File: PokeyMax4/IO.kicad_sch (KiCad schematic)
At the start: 2 parts

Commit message: Update the v4 board
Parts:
- R6: JLCPCB Part # C102771 -> (none); LCSC Part # (none) -> C25860
- R7: JLCPCB Part # C304991 -> (none); LCSC Part # (none) -> C25879
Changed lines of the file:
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@@
+	(wire
+		(pts
+			(xy 144.78 83.82) (xy 144.78 91.44)
+		)
+		(stroke
+			(width 0.1524)
+			(type solid)
+		)
+	)
+	(wire
+		(pts
+			(xy 144.78 119.38) (xy 144.78 121.92)
+		)
+		(stroke
+			(width 0.1524)
+			(type solid)
+		)
+	)
 	(wire
 		(pts
@@
 			(width 0.1524)
 			(type solid)
-		)
-	)
-	(wire
-		(pts
-			(xy 144.78 83.82) (xy 144.78 91.44)
-		)
-		(stroke
-			(width 0.1524)
-			(type solid)
-		)
-	)
-	(wire
-		(pts
-			(xy 144.78 119.38) (xy 144.78 121.92)
-		)
-		(stroke
-			(width 0.1524)
-			(type solid)
-		)
-	)
-	(global_label "3V3"
-		(shape bidirectional)
-		(at 144.78 83.82 0)
-		(fields_autoplaced yes)
-		(effects
-			(font
-				(size 1.2446 1.2446)
-			)
-			(justify left)
-		)
-		(property "Intersheetrefs" "${INTERSHEET_REFS}"
-			(at 152.2316 83.82 0)
-			(effects
-				(font
-					(size 1.27 1.27)
-				)
-				(justify left)
-				(hide yes)
-			)
 		)
 	)
@@
 				(justify left)
 				(hide yes)
+			)
+		)
+	)
+	(global_label "3V3"
+		(shape bidirectional)
+		(at 144.78 87.63 0)
+		(fields_autoplaced yes)
+		(effects
+			(font
+				(size 1.2446 1.2446)
+			)
+			(justify left)
+		)
+		(property "Intersheetrefs" "${INTERSHEET_REFS}"
+			(at 152.2316 87.63 0)
+			(effects
+				(font
+					(size 1.27 1.27)
+				)
+				(justify left)
+				(hide yes)
+			)
+		)
+	)
+	(symbol
+		(lib_id "pokeymax4-eagle-import:R-EU_R0402")
+		(at 144.78 96.52 90)
+		(unit 1)
+		(exclude_from_sim no)
+		(in_bom yes)
+		(on_board yes)
+		(dnp no)
+		(property "Reference" "R6"
+			(at 143.2814 100.33 0)
+			(effects
+				(font
+					(size 1.778 1.5113)
+				)
+				(justify left bottom)
+			)
+		)
+		(property "Value" "1k1"
+			(at 148.082 100.33 0)
+			(effects
+				(font
+					(size 1.778 1.5113)
+				)
+				(justify left bottom)
+			)
+		)
+		(property "Footprint" "pokeymax4:R0402"
+			(at 144.78 96.52 0)
+			(effects
+				(font
+					(size 1.27 1.27)
+				)
+				(hide yes)
+			)
+		)
+		(property "Datasheet" ""
+			(at 144.78 96.52 0)
+			(effects
+				(font
+					(size 1.27 1.27)
+				)
+				(hide yes)
+			)
+		)
+		(property "Description" ""
+			(at 144.78 96.52 0)
+			(effects
+				(font
+					(size 1.27 1.27)
+				)
+				(hide yes)
+			)
+		)
+		(property "LCSC Part #" "C25860"
+			(at 144.78 96.52 0)
+			(effects
+				(font
+					(size 1.27 1.27)
+				)
+				(hide yes)
+			)
+		)
+		(pin "1"
+		)
+		(pin "2"
+		)
+		(instances
+			(project ""
+				(path "/e6275eb3-d183-4a15-8a8c-dffc95cf456c/ffebd24f-75aa-4e21-be2c-b55208e79830"
+					(reference "R6")
+					(unit 1)
+				)
 			)
 		)
@@
 			)
 		)
-		(property "JLCPCB Position Offset" ""
-			(at 144.78 114.3 0)
-			(effects
-				(font
-					(size 1.27 1.27)
-				)
-				(hide yes)
-			)
-		)
-		(property "JLCPCB Rotation Offset" ""
-			(at 144.78 114.3 0)
-			(effects
-				(font
-					(size 1.27 1.27)
-				)
-				(hide yes)
-			)
-		)
-		(property "JLCPCB Part #" "C304991"
-			(at 144.78 114.3 0)
-			(effects
-				(font
-					(size 1.27 1.27)
-				)
-				(hide yes)
-			)
+		(property "LCSC Part #" " C25879"
+			(at 144.78 114.3 0)
+			(effects
+				(font
+					(size 1.27 1.27)
+				)
+				(hide yes)
+			)
+		)
+		(pin "1"
 		)
 		(pin "2"
 		)
-		(pin "1"
-		)
 		(instances
-			(project "pokeymax4"
-				(path "/87a5706b-9c3d-497f-99bc-f4f71751dafe/b931f0b5-7d10-4325-a72c-13a8b4fa7819"
+			(project ""
+				(path "/e6275eb3-d183-4a15-8a8c-dffc95cf456c/ffebd24f-75aa-4e21-be2c-b55208e79830"
 					(reference "R7")
 					(unit 1)
 				)
-			)
-		)
-	)
-	(symbol
-		(lib_id "pokeymax4-eagle-import:R-EU_R0402")
-		(at 144.78 96.52 90)
-		(unit 1)
-		(exclude_from_sim no)
-		(in_bom yes)
-		(on_board yes)
-		(dnp no)
-		(property "Reference" "R6"
-			(at 143.2814 100.33 0)
-			(effects
-				(font
-					(size 1.778 1.5113)
-				)
-				(justify left bottom)
-			)
-		)
-		(property "Value" "1k1"
-			(at 148.082 100.33 0)
-			(effects
-				(font
-					(size 1.778 1.5113)
-				)
-				(justify left bottom)
-			)
-		)
-		(property "Footprint" "pokeymax4:R0402"
-			(at 144.78 96.52 0)
-			(effects
-				(font
-					(size 1.27 1.27)
-				)
-				(hide yes)
-			)
-		)
-		(property "Datasheet" ""
-			(at 144.78 96.52 0)
-			(effects
-				(font
-					(size 1.27 1.27)
-				)
-				(hide yes)
-			)
-		)
-		(property "Description" ""
-			(at 144.78 96.52 0)
-			(effects
-				(font
-					(size 1.27 1.27)
-				)
-				(hide yes)
-			)
-		)
-		(property "JLCPCB Position Offset" ""
-			(at 144.78 96.52 0)
-			(effects
-				(font
-					(size 1.27 1.27)
-				)
-				(hide yes)
-			)
-		)
-		(property "JLCPCB Rotation Offset" ""
-			(at 144.78 96.52 0)
-			(effects
-				(font
-					(size 1.27 1.27)
-				)
-				(hide yes)
-			)
-		)
-		(property "JLCPCB Part #" "C102771"
-			(at 144.78 96.52 0)
-			(effects
-				(font
-					(size 1.27 1.27)
-				)
-				(hide yes)
-			)
-		)
-		(pin "1"
-		)
-		(pin "2"
-		)
-		(instances
-			(project "pokeymax4"
-				(path "/87a5706b-9c3d-497f-99bc-f4f71751dafe/b931f0b5-7d10-4325-a72c-13a8b4fa7819"
-					(reference "R6")
-					(unit 1)
-				)

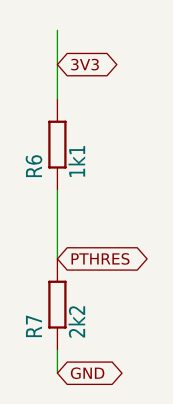
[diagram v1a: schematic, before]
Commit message: Updates for JLCPCB fabrication and parts library
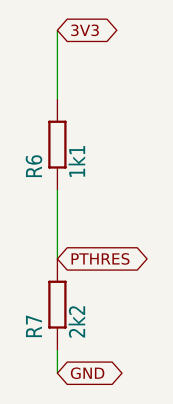
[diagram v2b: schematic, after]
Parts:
- R7: LCSC Part # C25879 -> C25879
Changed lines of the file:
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@@
 	(global_label "3V3"
 		(shape bidirectional)
-		(at 144.78 87.63 0)
+		(at 144.78 83.82 0)
 		(fields_autoplaced yes)
 		(effects
@@
 		)
 		(property "Intersheetrefs" "${INTERSHEET_REFS}"
-			(at 152.2316 87.63 0)
+			(at 152.2316 83.82 0)
 			(effects
 				(font
@@
 		)
 		(property "LCSC Part #" "C25860"
+			(at 144.78 96.52 0)
+			(effects
+				(font
+					(size 1.27 1.27)
+				)
+				(hide yes)
+			)
+		)
+		(property "JLCPCB Rotation Offset" ""
 			(at 144.78 96.52 0)
 			(effects
@@
 			)
 		)
-		(property "LCSC Part #" " C25879"
+		(property "LCSC Part #" "C25879"
 			(at 144.78 114.3 0)
 			(effects
+				(font
+					(size 1.27 1.27)
+				)
+				(hide yes)
+			)
+		)
+		(property "JLCPCB Rotation Offset" ""
+			(at 144.78 114.3 0)
+			(effects

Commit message: Update BOM from 0402 to 0603 where relevant
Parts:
- R6: LCSC Part # C25860 -> C140120
- R7: LCSC Part # C25879 -> C294652
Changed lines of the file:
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@@
 			)
 		)
-		(property "LCSC Part #" "C25860"
+		(property "LCSC Part #" "C140120"
 			(at 144.78 96.52 0)
 			(effects
@@
 			)
 		)
-		(property "LCSC Part #" "C25879"
+		(property "LCSC Part #" "C294652"
 			(at 144.78 114.3 0)
 			(effects
